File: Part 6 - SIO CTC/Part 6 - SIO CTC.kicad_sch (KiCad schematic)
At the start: 50 parts, among them J1 EDGE, U1 74AHC00, U10 SST39SF010, U11 AS6C4008, U2 74AHC32, U3 74AHC32, U4 74AHC32, U5 74HC563, U6 74AHC174, U7 74AHC138, U8 Z80C0010, U9 74HC563

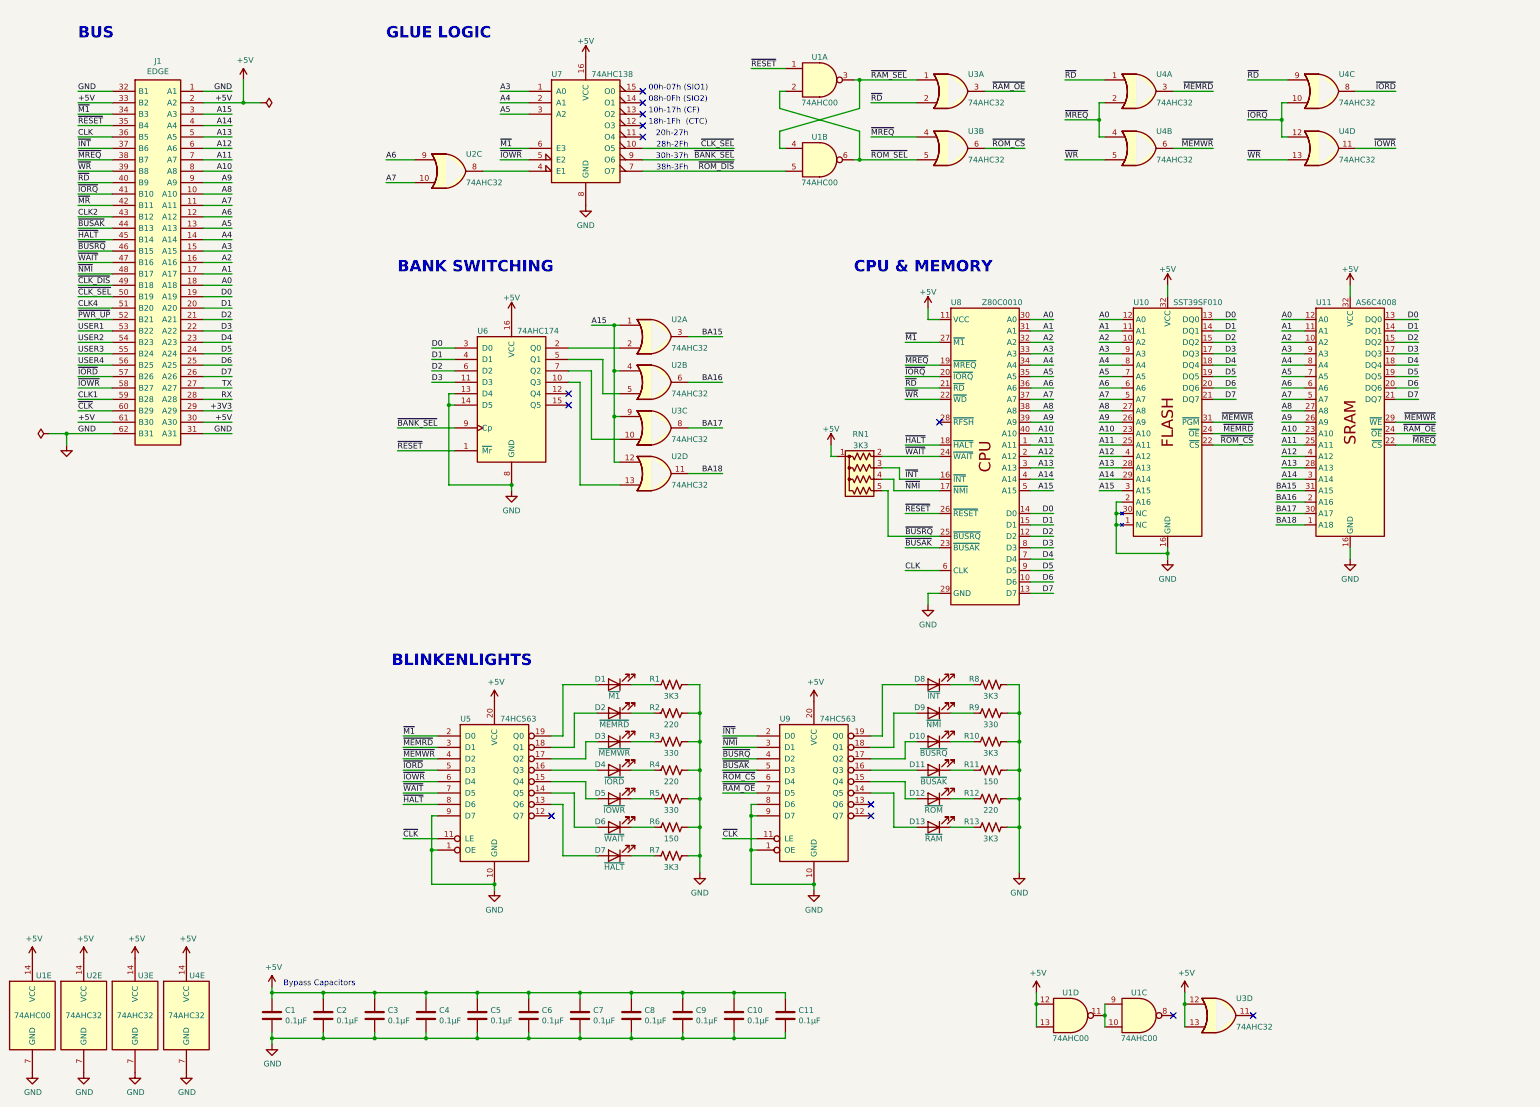
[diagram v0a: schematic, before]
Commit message: Updated clock, and created CPU card
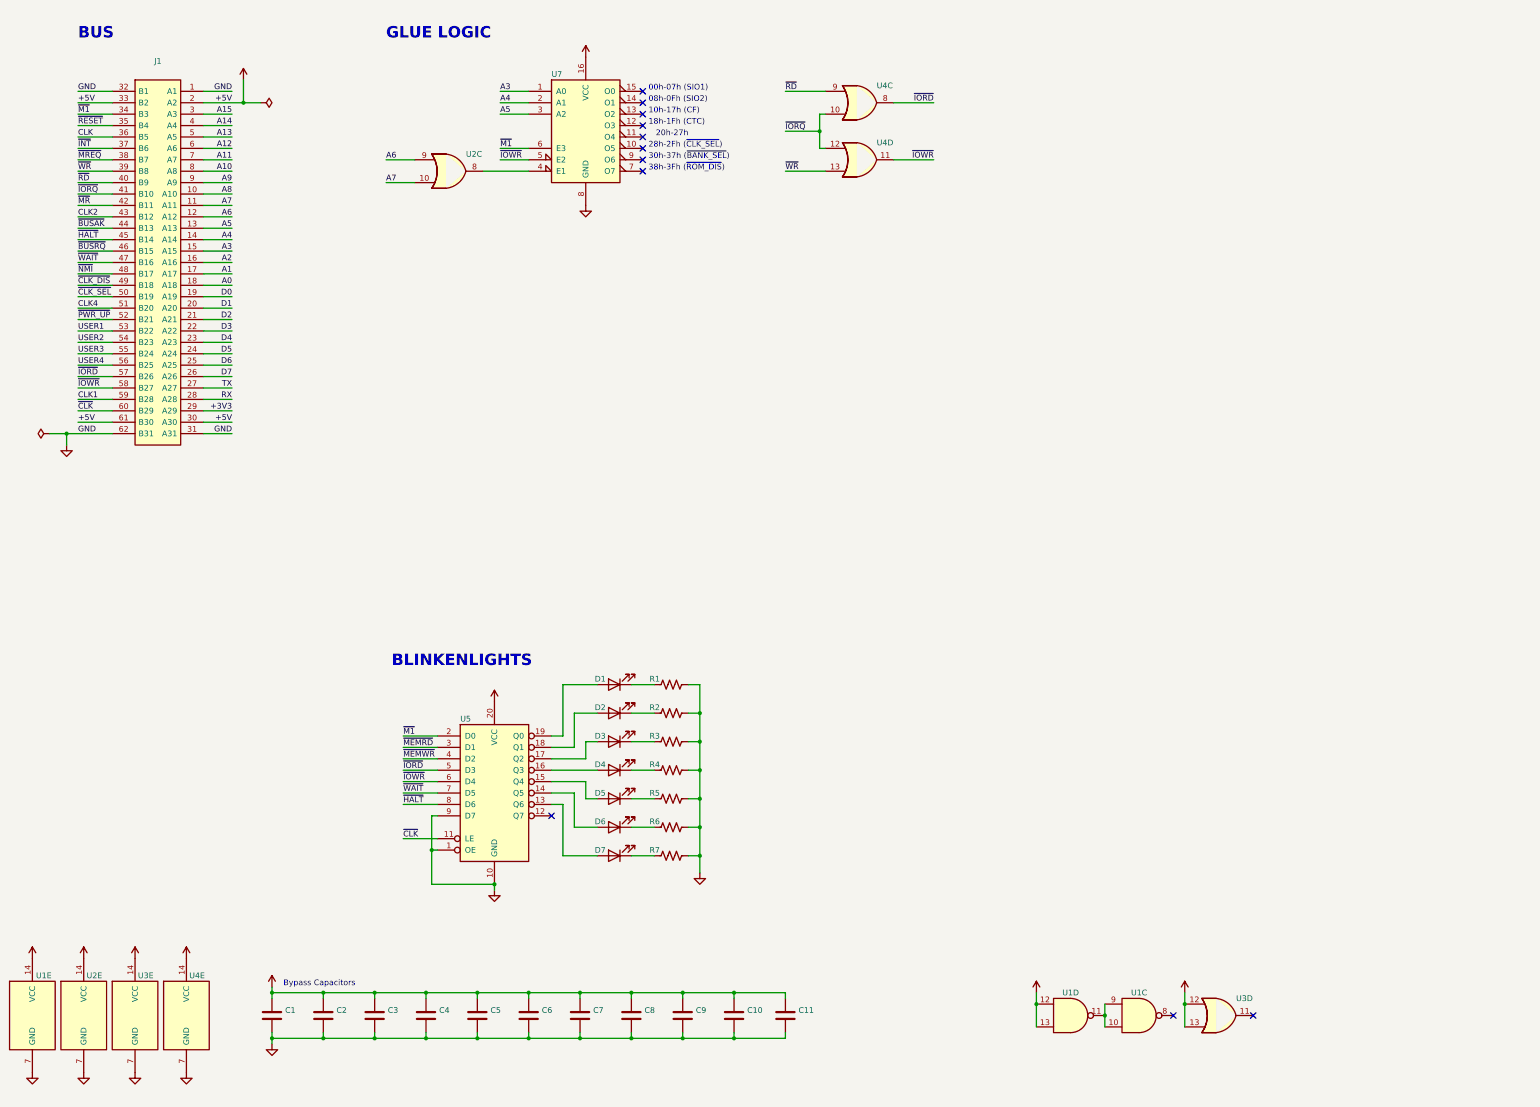
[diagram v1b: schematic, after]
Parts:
- removed D10: ~{BUSRQ}, LED_THT:LED_D3.0mm_Horizontal_O1.27mm_Z2.0mm_Clear, symbol Device:LED
- removed D11: ~{BUSAK}, LED_THT:LED_D3.0mm_Horizontal_O1.27mm_Z2.0mm_Clear, symbol Device:LED
- removed D12: ~{ROM}, LED_THT:LED_D3.0mm_Horizontal_O1.27mm_Z2.0mm_Clear, symbol Device:LED
- removed D13: ~{RAM}, LED_THT:LED_D3.0mm_Horizontal_O1.27mm_Z2.0mm_Clear, symbol Device:LED
- removed D8: ~{INT}, LED_THT:LED_D3.0mm_Horizontal_O1.27mm_Z2.0mm_Clear, symbol Device:LED
- removed D9: ~{NMI}, LED_THT:LED_D3.0mm_Horizontal_O1.27mm_Z2.0mm_Clear, symbol Device:LED
- removed R10, R13, R8: 3K3, Resistor_THT:R_Axial_DIN0207_L6.3mm_D2.5mm_P10.16mm_Horizontal, symbol Device:R_US
- removed R11: 150, Resistor_THT:R_Axial_DIN0207_L6.3mm_D2.5mm_P10.16mm_Horizontal, symbol Device:R_US
- removed R12: 220, Resistor_THT:R_Axial_DIN0207_L6.3mm_D2.5mm_P10.16mm_Horizontal, symbol Device:R_US
- removed R9: 330, Resistor_THT:R_Axial_DIN0207_L6.3mm_D2.5mm_P10.16mm_Horizontal, symbol Device:R_US
- removed RN1: 3K3, Resistor_THT:R_Array_SIP5, symbol Device:R_Network04_US
- removed unit 1 of U1
- removed unit 2 of U1
- removed U10: SST39SF010, Package_DIP:DIP-32_W15.24mm_Socket, symbol 0_Z80_Library:SST39SF010
- removed U11: AS6C4008, Package_DIP:DIP-32_W15.24mm_Socket, symbol 0_Z80_Library:AS6C4008
- removed unit 4 of U2
- removed unit 1 of U2
- removed unit 2 of U2
- removed unit 3 of U3
- removed unit 1 of U3
- removed unit 2 of U3
- removed unit 2 of U4
- removed unit 1 of U4
- removed U6: 74AHC174, Package_DIP:DIP-16_W7.62mm_Socket, symbol 74xx:74LS174
- removed U8: Z80C0010, Package_DIP:DIP-40_W15.24mm_Socket, symbol 0_Z80_Library:Z80C00xx
- removed U9: 74HC563, Package_DIP:DIP-20_W7.62mm_Socket, symbol 0_Z80_Library:74HC563
- C1, C10, C11, C2, C3, C4, C5, C6, C7, C8, C9: value 0.1µF -> (none); footprint Capacitor_THT:C_Disc_D3.0mm_W1.6mm_P2.50mm -> (none)
- D1: value ~{M1} -> (none); footprint LED_THT:LED_D3.0mm_Horizontal_O1.27mm_Z2.0mm_Clear -> (none)
- D2: value ~{MEMRD} -> (none); footprint LED_THT:LED_D3.0mm_Horizontal_O1.27mm_Z2.0mm_Clear -> (none)
- D3: value ~{MEMWR} -> (none); footprint LED_THT:LED_D3.0mm_Horizontal_O1.27mm_Z2.0mm_Clear -> (none)
- D4: value ~{IORD} -> (none); footprint LED_THT:LED_D3.0mm_Horizontal_O1.27mm_Z2.0mm_Clear -> (none)
- D5: value ~{IOWR} -> (none); footprint LED_THT:LED_D3.0mm_Horizontal_O1.27mm_Z2.0mm_Clear -> (none)
- D6: value ~{WAIT} -> (none); footprint LED_THT:LED_D3.0mm_Horizontal_O1.27mm_Z2.0mm_Clear -> (none)
- D7: value ~{HALT} -> (none); footprint LED_THT:LED_D3.0mm_Horizontal_O1.27mm_Z2.0mm_Clear -> (none)
- J1: value EDGE -> (none); footprint 0_Z80_Library:BUS_XT -> (none)
- R1, R7: value 3K3 -> (none); footprint Resistor_THT:R_Axial_DIN0207_L6.3mm_D2.5mm_P10.16mm_Horizontal -> (none)
- R2, R4: value 220 -> (none); footprint Resistor_THT:R_Axial_DIN0207_L6.3mm_D2.5mm_P10.16mm_Horizontal -> (none)
- R3, R5: value 330 -> (none); footprint Resistor_THT:R_Axial_DIN0207_L6.3mm_D2.5mm_P10.16mm_Horizontal -> (none)
- R6: value 150 -> (none); footprint Resistor_THT:R_Axial_DIN0207_L6.3mm_D2.5mm_P10.16mm_Horizontal -> (none)
- U1: value 74AHC00 -> (none); footprint Package_DIP:DIP-14_W7.62mm_Socket -> (none)
- U2, U3, U4: value 74AHC32 -> (none); footprint Package_DIP:DIP-14_W7.62mm_Socket -> (none)
- U5: value 74HC563 -> (none); footprint Package_DIP:DIP-20_W7.62mm_Socket -> (none)
- U7: value 74AHC138 -> (none); footprint Package_DIP:DIP-16_W7.62mm_Socket -> (none)
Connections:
- net ~{CLK_SEL}: no longer U7.10 (O5)
- net ~{BANK_SEL}: no longer names the net of U7.9 (O6)
- net ~{ROM_DIS}: no longer names the net of U7.7 (O7)
- no-connect marks 13 -> 11
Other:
- note added: "28h-2Fh (~{CLK_SEL})"
- note added: "30h-37h (~{BANK_SEL})"
- note added: "38h-3Fh (~{ROM_DIS})"
- note removed: "28h-2Fh"
- note removed: "30h-37h"
- note removed: "38h-3Fh"
- note removed: "BANK SWITCHING"
- note removed: "CPU & MEMORY"
- company: Frederic Segard, aka: The Micro Hobbyist -> Frédéric Segard a.k.a. Micro Hobbyist
- title: CPU,  64K FLASH, 512K RAM, with blinkenlights -> SIO and CTC
- moved on the sheet: U4C, U4D

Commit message: Changed the clock for even cleaner clock switching
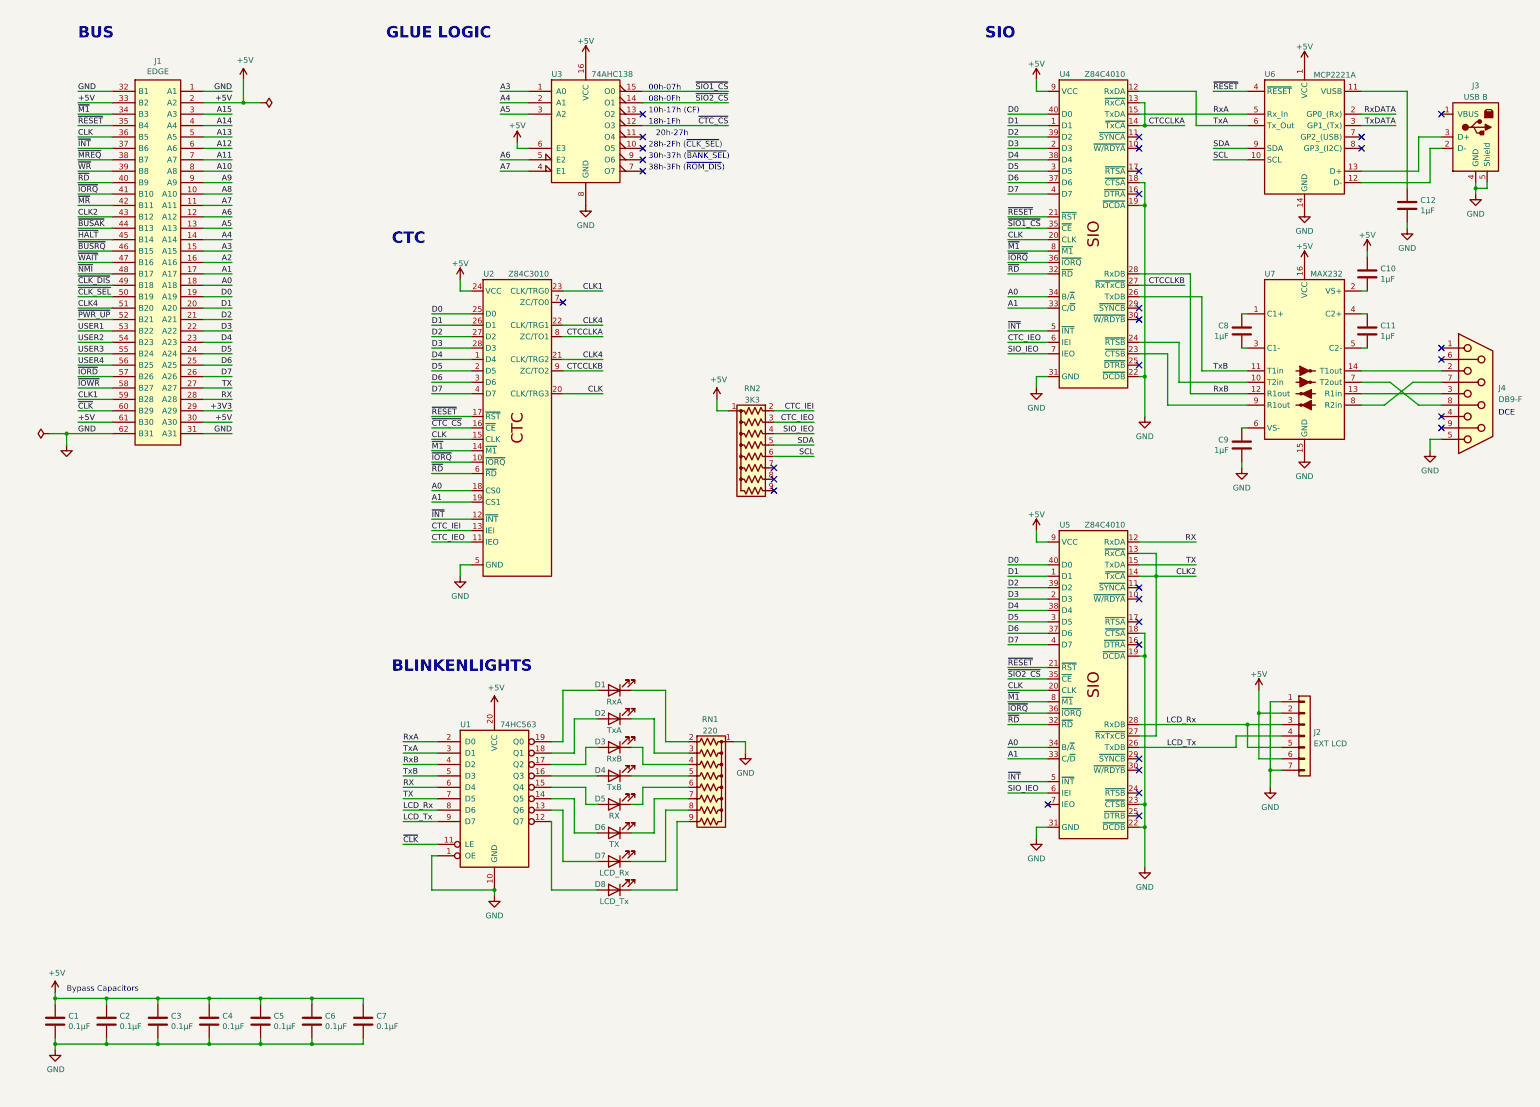
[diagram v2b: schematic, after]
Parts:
- removed R1, R2, R3, R4, R5, R6, R7: (no value), symbol Device:R_US
- removed U1: (no value), symbol 74xx:74HC00
- removed U2, U3, U4: (no value), symbol 74xx:74LS32
- added C12: 1µF, Capacitor_THT:C_Disc_D3.0mm_W1.6mm_P2.50mm, symbol Device:C
- added D8: LCD_Tx, LED_THT:LED_D3.0mm_Horizontal_O1.27mm_Z2.0mm_Clear, symbol Device:LED
- added J2: EXT LCD, Connector_PinHeader_2.54mm:PinHeader_1x07_P2.54mm_Horizontal, symbol Connector_Generic:Conn_01x07
- added J3: USB B, Connector_USB:USB_B_Lumberg_2411_02_Horizontal, symbol 0_Z80_Library:USB_B
- added J4: DB9-F, Connector_Dsub:DSUB-9_Female_Horizontal_P2.77x2.84mm_EdgePinOffset7.70mm_Housed_MountingHolesOffset9.12mm, symbol Connector:DB9_Female
- added RN1: 220, Resistor_THT:R_Array_SIP9, symbol Device:R_Network08_US
- added RN2: 3K3, Resistor_THT:R_Array_SIP9, symbol Device:R_Network08_US
- added U2: Z84C3010, Package_DIP:DIP-28_W15.24mm_Socket, symbol 0_Z80_Library:Z84C30xx CTC
- added U4, U5: Z84C4010, Package_DIP:DIP-40_W15.24mm_Socket, symbol 0_Z80_Library:Z84C40xx SIO
- added U6: MCP2221A, Package_DIP:DIP-14_W7.62mm_Socket, symbol 0_Z80_Library:MCP2221A
- added U7: MAX232, Package_DIP:DIP-16_W7.62mm_Socket, symbol 0_Z80_Library:MAX232
- C1, C2, C3, C4, C5, C6, C7: value (none) -> 0.1µF; footprint (none) -> Capacitor_THT:C_Disc_D3.0mm_W1.6mm_P2.50mm
- C10, C11, C8, C9: value (none) -> 1µF; footprint (none) -> Capacitor_THT:C_Disc_D3.0mm_W1.6mm_P2.50mm
- D1: value (none) -> RxA; footprint (none) -> LED_THT:LED_D3.0mm_Horizontal_O1.27mm_Z2.0mm_Clear
- D2: value (none) -> TxA; footprint (none) -> LED_THT:LED_D3.0mm_Horizontal_O1.27mm_Z2.0mm_Clear
- D3: value (none) -> RxB; footprint (none) -> LED_THT:LED_D3.0mm_Horizontal_O1.27mm_Z2.0mm_Clear
- D4: value (none) -> TxB; footprint (none) -> LED_THT:LED_D3.0mm_Horizontal_O1.27mm_Z2.0mm_Clear
- D5: value (none) -> RX; footprint (none) -> LED_THT:LED_D3.0mm_Horizontal_O1.27mm_Z2.0mm_Clear
- D6: value (none) -> TX; footprint (none) -> LED_THT:LED_D3.0mm_Horizontal_O1.27mm_Z2.0mm_Clear
- D7: value (none) -> LCD_Rx; footprint (none) -> LED_THT:LED_D3.0mm_Horizontal_O1.27mm_Z2.0mm_Clear
- J1: value (none) -> EDGE; footprint (none) -> 0_Z80_Library:BUS_XT
- U1: renamed from U5; value (none) -> 74HC563; footprint (none) -> Package_DIP:DIP-20_W7.62mm_Socket
- U3: renamed from U7; value (none) -> 74AHC138; footprint (none) -> Package_DIP:DIP-16_W7.62mm_Socket
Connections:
- net +5V: now also U3.6 (E3), J2.2 (Pin_2), J2.6 (Pin_6), RN2.1 (common), U2.24 (VCC), U4.9 (VCC), U5.9 (VCC), U6.1 (VCC), U7.16 (VCC); no longer C11.1, C8.1, C9.1
- net A0: now also U2.18 (CS0), U4.34 (B/~{A}), U5.34 (B/~{A})
- net A1: now also U2.19 (CS1), U4.33 (C/~{D}), U5.33 (C/~{D})
- net A6: now also U3.5 (E2)
- net A7: now also U3.4 (E1)
- net CLK: now also U2.15 (CLK), U2.20 (CLK/TRG3), U4.20 (CLK), U5.20 (CLK)
- net CLK1: now also U2.23 (CLK/TRG0)
- net CLK2: now also U5.13 (~{RxCA}), U5.14 (~{TxCA}), U5.27 (~{RxTxCB})
- net CLK4: now also U2.21 (CLK/TRG2), U2.22 (CLK/TRG1)
- net D0: now also U2.25 (D0), U4.40 (D0), U5.40 (D0)
- net D1: now also U2.26 (D1), U4.1 (D1), U5.1 (D1)
- net D2: now also U2.27 (D2), U4.39 (D2), U5.39 (D2)
- net D3: now also U2.28 (D3), U4.2 (D3), U5.2 (D3)
- net D4: now also U2.1 (D4), U4.38 (D4), U5.38 (D4)
- net D5: now also U2.2 (D5), U4.3 (D5), U5.3 (D5)
- net D6: now also U2.3 (D6), U4.37 (D6), U5.37 (D6)
- net D7: now also U2.4 (D7), U4.4 (D7), U5.4 (D7)
- net GND: now also C12.2, J2.1 (Pin_1), J2.7 (Pin_7), J3.4 (GND), J3.5 (Shield), J4.5, RN1.1 (common), U2.5 (GND), U4.18 (~{CTSA}), U4.19 (~{DCDA}), U4.22 (~{DCDB}), U4.31 (GND), U5.18 (~{CTSA}), U5.19 (~{DCDA}), U5.22 (~{DCDB}), U5.23 (~{CTSB}), U5.31 (GND), U6.14 (GND), U7.15 (GND); no longer C10.2, C11.2, C8.2, U1.9 (D7)
- net RX: now also U1.6 (D4), U5.12 (RxDA)
- net TX: now also U1.7 (D5), U5.15 (TxDA)
- net ~{HALT}: no longer U1.8 (D6)
- net ~{INT}: now also U2.12 (~{INT}), U4.5 (~{INT}), U5.5 (~{INT})
- net ~{IORD}: no longer U1.5 (D3)
- net ~{IORQ}: now also U2.10 (~{IORQ}), U4.36 (~{IORQ}), U5.36 (~{IORQ})
- net ~{IOWR}: no longer U1.6 (D4), U3.5 (E2)
- net ~{M1}: now also U2.14 (~{M1}), U4.8 (~{M1}), U5.8 (~{M1}); no longer U1.2 (D0), U3.6 (E3)
- net ~{RD}: now also U2.6 (~{RD}), U4.32 (~{RD}), U5.32 (~{RD})
- net ~{RESET}: now also U2.17 (~{RST}), U4.21 (~{RST}), U5.21 (~{RST}), U6.4 (~{RESET})
- net ~{WAIT}: no longer U1.7 (D5)
- net at D2.1 (K): now also RN1.3 (R2)
- net at D6.1 (K): now also RN1.7 (R6)
- net at D3.1 (K): now also RN1.4 (R3)
- net at U1.12 (Q7): now also D8.2 (A)
- net at D4.1 (K): now also RN1.5 (R4)
- net ~{CTC_CS}: now reaches U3.12 (O3)
- net ~{CTC_CS}: now also U2.16 (~{CE})
- net ~{SIO2_CS}: now reaches U3.14 (O1)
- net ~{SIO2_CS}: now also U5.35 (~{CE})
- net ~{SIO1_CS}: now reaches U3.15 (O0)
- net ~{SIO1_CS}: now also U4.35 (~{CE})
- net at D7.1 (K): now also RN1.8 (R7)
- net at D5.1 (K): now also RN1.6 (R5)
- net at D1.1 (K): now also RN1.2 (R1)
- net ~{MEMRD} renamed TxA
- net TxA: now also U4.12 (RxDA), U6.6 (Tx_Out)
- net ~{MEMWR} renamed RxB
- net RxB: now also U4.28 (RxDB), U7.12 (R1out)
- new net: J3.2 (D-), U6.12 (D-)
- new net: J3.3 (D+), U6.13 (D+)
- new net: C12.1, U6.11 (VUSB)
- new net: D8.1 (K), RN1.9 (R8)
- new net: C9.1, U7.6 (VS-)
- new net: C8.1, U7.1 (C1+)
- new net: U4.24 (~{RTSB}), U7.10 (T2in)
- new net: J4.3, U7.13 (R1in)
- new net: J4.2, U7.14 (T1out)
- new net: C10.2, U7.2 (VS+)
- new net: C8.2, U7.3 (C1-)
- new net: C11.1, U7.4 (C2+)
- new net: C11.2, U7.5 (C2-)
- new net: J4.8, U7.7 (T2out)
- new net: J4.7, U7.8 (R2in)
- new net: U4.23 (~{CTSB}), U7.9 (R1out)
- new net CTCCLKA: U2.8 (ZC/TO1), U4.13 (~{RxCA}), U4.14 (~{TxCA})
- new net CTCCLKB: U2.9 (ZC/TO2), U4.27 (~{RxTxCB})
- new net CTC_IEI: RN2.2 (R1), U2.13 (IEI)
- new net CTC_IEO: RN2.3 (R2), U2.11 (IEO), U4.6 (IEI)
- new net LCD_Rx: J2.3 (Pin_3), J2.5 (Pin_5), U1.8 (D6), U5.28 (RxDB)
- new net LCD_Tx: J2.4 (Pin_4), U1.9 (D7), U5.26 (TxDB)
- new net RxA: U1.2 (D0), U4.15 (TxDA), U6.5 (Rx_In)
- new net RxDATA: U6.2 (GP0_(Rx))
- new net SCL: RN2.6 (R5), U6.10 (SCL)
- new net SDA: RN2.5 (R4), U6.9 (SDA)
- new net SIO_IEO: RN2.4 (R3), U4.7 (IEO), U5.6 (IEI)
- new net TxB: U1.5 (D3), U4.26 (TxDB), U7.11 (T1in)
- new net TxDATA: U6.3 (GP1_(Tx))
- no-connect marks 11 -> 32
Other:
- note added: "00h-07h"
- note added: "08h-0Fh"
- note added: "18h-1Fh"
- note added: "CTC"
- note added: "DCE"
- note added: "SIO"
- note removed: "00h-07h (SIO1)"
- note removed: "08h-0Fh (SIO2)"
- note removed: "18h-1Fh (CTC)"
- moved on the sheet: C1, C2, C3, C4, C5, C6, C7, D1, D2, D3, D4, D5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

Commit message: Added Keyboard, and minor fixes
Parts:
- U3: value 74AHC138 -> 74AC138
- renumbered C12 to C1, C5 to C10, C6 to C11, C7 to C12, C10 to C2, C8 to C3, C11 to C4, C9 to C5, C1 to C6, C2 to C7, C3 to C8, C4 to C9, J3 to J2, J4 to J3, J2 to J4, RN2 to RN1, RN1 to RN2, U4 to U1, U6 to U2, U7 to U4, U2 to U5, U5 to U6, U1 to U7
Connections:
- net ~{IORD} renamed USER5
- net ~{IOWR} renamed USER6
